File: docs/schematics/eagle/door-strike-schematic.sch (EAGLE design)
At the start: 9 parts, among them T1 TIP120

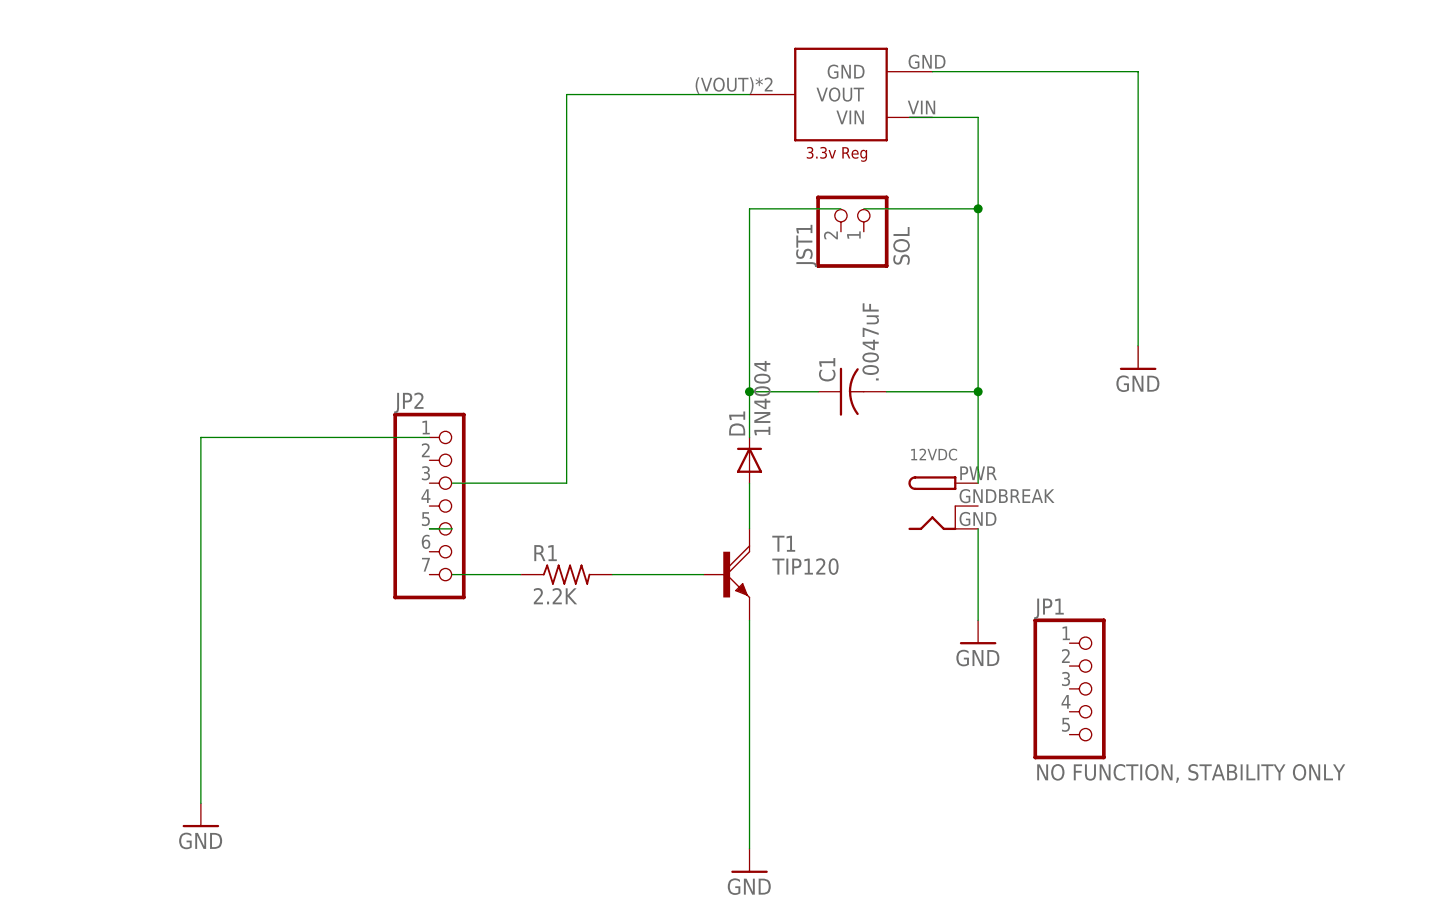
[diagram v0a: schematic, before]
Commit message: updated schema with RFduino component and caps for voltage regulation
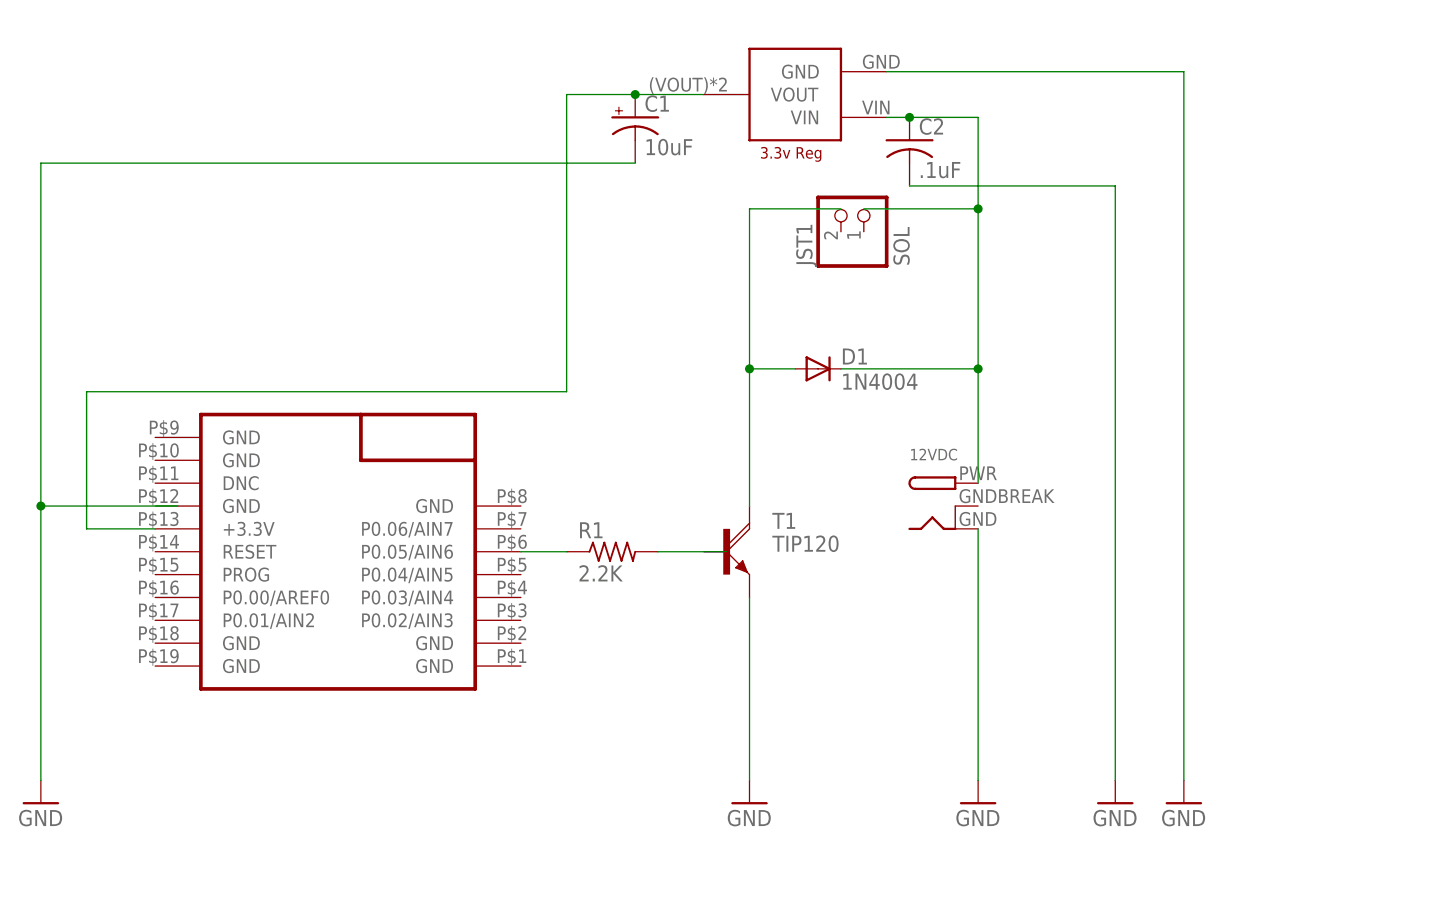
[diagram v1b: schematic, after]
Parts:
- removed JP1: NO FUNCTION, STABILITY ONLY, pinhead:PINHD-1X5
- removed JP2: (no value), pinhead:PINHD-1X7
- added C2: .1uF, adafruit:C-US102-054X133
- added U$2: RFD22301, RFD22301-11.25.13:RFD22301
- C1: value .0047uF -> 10uF; device adafruit:C-US025-024X044 -> adafruit:CPOL-USE2-5
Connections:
- removed net N$5: JP2.5
- removed net N$6 (its old number): C1.1, D1.C
- net GND: now also C1.-, C2.2; no longer JP2.1
- net N$1: now also R1.1, U$2.P0.05/AIN6; no longer R1.2, T1.B
- net N$2: now also R1.2; no longer R1.1
- net N$7: now also C1.+, U$2.+3.3V
- net N$8: now also C2.1, D1.C, U$1.VIN; no longer C1.2
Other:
- moved on the sheet: D1, R1, T1
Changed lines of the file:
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@@
 <part name="JST1" library="adafruit" deviceset="JST_2PIN" device="-THM" value="SOL"/>
 <part name="GND1" library="supply1" deviceset="GND" device=""/>
-<part name="JP1" library="pinhead" deviceset="PINHD-1X5" device="" value="NO FUNCTION, STABILITY ONLY"/>
-<part name="JP2" library="pinhead" deviceset="PINHD-1X7" device=""/>
 <part name="GND2" library="supply1" deviceset="GND" device=""/>
 <part name="12VDC" library="adafruit" deviceset="DCBARREL" device="PTH"/>
@@
 <part name="GND3" library="supply1" deviceset="GND" device=""/>
 <part name="GND4" library="supply1" deviceset="GND" device=""/>
-<part name="C1" library="adafruit" deviceset="C-US" device="025-024X044" value=".0047uF"/>
+<part name="C1" library="adafruit" deviceset="CPOL-US" device="E2-5" value="10uF"/>
+<part name="C2" library="adafruit" deviceset="C-US" device="102-054X133" value=".1uF"/>
+<part name="GND5" library="supply1" deviceset="GND" device=""/>
+<part name="U$2" library="RFD22301-11.25.13" deviceset="RFD22301" device=""/>
 </parts>
 <sheets>
@@
 </plain>
 <instances>
-<instance part="T1" gate="1" x="48.26" y="50.8"/>
-<instance part="R1" gate="G$1" x="30.48" y="50.8"/>
-<instance part="D1" gate="1" x="50.8" y="63.5" rot="R90"/>
+<instance part="T1" gate="1" x="48.26" y="53.34"/>
+<instance part="R1" gate="G$1" x="35.56" y="53.34"/>
+<instance part="D1" gate="1" x="58.42" y="73.66"/>
 <instance part="JST1" gate="G$1" x="63.5" y="91.44" rot="R90"/>
-<instance part="GND1" gate="1" x="50.8" y="17.78"/>
-<instance part="JP1" gate="A" x="88.9" y="38.1"/>
-<instance part="JP2" gate="A" x="17.78" y="58.42"/>
-<instance part="GND2" gate="1" x="-10.16" y="22.86"/>
+<instance part="GND1" gate="1" x="50.8" y="25.4"/>
+<instance part="GND2" gate="1" x="-27.94" y="25.4"/>
 <instance part="12VDC" gate="G$1" x="73.66" y="58.42"/>
-<instance part="U$1" gate="G$1" x="60.96" y="104.14" rot="R180"/>
-<instance part="GND3" gate="1" x="93.98" y="73.66"/>
-<instance part="GND4" gate="1" x="76.2" y="43.18"/>
-<instance part="C1" gate="G$1" x="60.96" y="71.12" rot="R90"/>
+<instance part="U$1" gate="G$1" x="55.88" y="104.14" rot="R180"/>
+<instance part="GND3" gate="1" x="99.06" y="25.4"/>
+<instance part="GND4" gate="1" x="76.2" y="25.4"/>
+<instance part="C1" gate="G$1" x="38.1" y="101.6"/>
+<instance part="C2" gate="G$1" x="68.58" y="99.06"/>
+<instance part="GND5" gate="1" x="91.44" y="25.4"/>
+<instance part="U$2" gate="G$1" x="5.08" y="53.34" rot="R180"/>
 </instances>
 <busses>
 </busses>
 <nets>
-<net name="N$1" class="0">
-<segment>
-<pinref part="R1" gate="G$1" pin="2"/>
-<pinref part="T1" gate="1" pin="B"/>
-<wire x1="35.56" y1="50.8" x2="45.72" y2="50.8" width="0.1524" layer="91"/>
-</segment>
-</net>
 <net name="GND" class="0">
 <segment>
 <pinref part="T1" gate="1" pin="E"/>
 <pinref part="GND1" gate="1" pin="GND"/>
-<wire x1="50.8" y1="45.72" x2="50.8" y2="20.32" width="0.1524" layer="91"/>
+<wire x1="50.8" y1="48.26" x2="50.8" y2="27.94" width="0.1524" layer="91"/>
 </segment>
 <segment>
 <pinref part="GND2" gate="1" pin="GND"/>
-<wire x1="-10.16" y1="25.4" x2="-10.16" y2="66.04" width="0.1524" layer="91"/>
-<pinref part="JP2" gate="A" pin="1"/>
-<wire x1="-10.16" y1="66.04" x2="15.24" y2="66.04" width="0.1524" layer="91"/>
+<wire x1="-27.94" y1="27.94" x2="-27.94" y2="58.42" width="0.1524" layer="91"/>
+<pinref part="C1" gate="G$1" pin="-"/>
+<wire x1="-27.94" y1="58.42" x2="-27.94" y2="96.52" width="0.1524" layer="91"/>
+<wire x1="38.1" y1="96.52" x2="-27.94" y2="96.52" width="0.1524" layer="91"/>
+<wire x1="-27.94" y1="58.42" x2="-12.7" y2="58.42" width="0.1524" layer="91"/>
+<junction x="-27.94" y="58.42"/>
 </segment>
 <segment>
 <pinref part="U$1" gate="G$1" pin="GND"/>
-<wire x1="71.12" y1="106.68" x2="93.98" y2="106.68" width="0.1524" layer="91"/>
-<wire x1="93.98" y1="106.68" x2="93.98" y2="76.2" width="0.1524" layer="91"/>
+<wire x1="66.04" y1="106.68" x2="99.06" y2="106.68" width="0.1524" layer="91"/>
+<wire x1="99.06" y1="106.68" x2="99.06" y2="27.94" width="0.1524" layer="91"/>
 <pinref part="GND3" gate="1" pin="GND"/>
 </segment>
 <segment>
 <pinref part="12VDC" gate="G$1" pin="GND"/>
-<wire x1="76.2" y1="55.88" x2="76.2" y2="45.72" width="0.1524" layer="91"/>
+<wire x1="76.2" y1="55.88" x2="76.2" y2="27.94" width="0.1524" layer="91"/>
 <pinref part="GND4" gate="1" pin="GND"/>
 </segment>
-</net>
-<net name="N$3" class="0">
 <segment>
-<pinref part="T1" gate="1" pin="C"/>
-<pinref part="D1" gate="1" pin="A"/>
-<wire x1="50.8" y1="55.88" x2="50.8" y2="60.96" width="0.1524" layer="91"/>
+<pinref part="C2" gate="G$1" pin="2"/>
+<wire x1="68.58" y1="93.98" x2="91.44" y2="93.98" width="0.1524" layer="91"/>
+<wire x1="91.44" y1="93.98" x2="91.44" y2="27.94" width="0.1524" layer="91"/>
+<pinref part="GND5" gate="1" pin="GND"/>
 </segment>
 </net>
@@
 <segment>
 <pinref part="12VDC" gate="G$1" pin="PWR"/>
-<wire x1="76.2" y1="60.96" x2="76.2" y2="71.12" width="0.1524" layer="91"/>
-<wire x1="76.2" y1="71.12" x2="76.2" y2="91.44" width="0.1524" layer="91"/>
+<wire x1="76.2" y1="60.96" x2="76.2" y2="73.66" width="0.1524" layer="91"/>
+<wire x1="76.2" y1="73.66" x2="76.2" y2="91.44" width="0.1524" layer="91"/>
 <wire x1="63.5" y1="91.44" x2="76.2" y2="91.44" width="0.1524" layer="91"/>
-<wire x1="76.2" y1="91.44" x2="76.2" y2="101.6" width="0.1524" layer="91"/>
+<pinref part="U$1" gate="G$1" pin="VIN"/>
+<wire x1="66.04" y1="101.6" x2="68.58" y2="101.6" width="0.1524" layer="91"/>
+<wire x1="68.58" y1="101.6" x2="76.2" y2="101.6" width="0.1524" layer="91"/>
+<wire x1="76.2" y1="101.6" x2="76.2" y2="91.44" width="0.1524" layer="91"/>
 <junction x="76.2" y="91.44"/>
-<wire x1="76.2" y1="101.6" x2="68.58" y2="101.6" width="0.1524" layer="91"/>
-<pinref part="C1" gate="G$1" pin="2"/>
-<wire x1="66.04" y1="71.12" x2="76.2" y2="71.12" width="0.1524" layer="91"/>
-<junction x="76.2" y="71.12"/>
-</segment>
-</net>
-<net name="N$2" class="0">
-<segment>
-<pinref part="R1" gate="G$1" pin="1"/>
-<wire x1="25.4" y1="50.8" x2="17.78" y2="50.8" width="0.1524" layer="91"/>
-</segment>
-</net>
-<net name="N$5" class="0">
-<segment>
-<wire x1="17.78" y1="55.88" x2="15.24" y2="55.88" width="0.1524" layer="91"/>
-<pinref part="JP2" gate="A" pin="5"/>
+<pinref part="C2" gate="G$1" pin="1"/>
+<junction x="68.58" y="101.6"/>
+<pinref part="D1" gate="1" pin="C"/>
+<wire x1="60.96" y1="73.66" x2="76.2" y2="73.66" width="0.1524" layer="91"/>
+<junction x="76.2" y="73.66"/>
 </segment>
 </net>
@@
 <segment>
 <pinref part="U$1" gate="G$1" pin="VOUT"/>
-<wire x1="50.8" y1="104.14" x2="30.48" y2="104.14" width="0.1524" layer="91"/>
-<wire x1="30.48" y1="104.14" x2="30.48" y2="60.96" width="0.1524" layer="91"/>
-<wire x1="30.48" y1="60.96" x2="17.78" y2="60.96" width="0.1524" layer="91"/>
+<wire x1="45.72" y1="104.14" x2="38.1" y2="104.14" width="0.1524" layer="91"/>
+<wire x1="38.1" y1="104.14" x2="30.48" y2="104.14" width="0.1524" layer="91"/>
+<wire x1="30.48" y1="104.14" x2="30.48" y2="71.12" width="0.1524" layer="91"/>
+<pinref part="C1" gate="G$1" pin="+"/>
+<junction x="38.1" y="104.14"/>
+<wire x1="30.48" y1="71.12" x2="-22.86" y2="71.12" width="0.1524" layer="91"/>
+<wire x1="-22.86" y1="71.12" x2="-22.86" y2="55.88" width="0.1524" layer="91"/>
+<pinref part="U$2" gate="G$1" pin="+3.3V"/>
+<wire x1="-22.86" y1="55.88" x2="-15.24" y2="55.88" width="0.1524" layer="91"/>
 </segment>
 </net>
@@
 <segment>
 <wire x1="50.8" y1="91.44" x2="60.96" y2="91.44" width="0.1524" layer="91"/>
-<pinref part="D1" gate="1" pin="C"/>
-<wire x1="50.8" y1="66.04" x2="50.8" y2="71.12" width="0.1524" layer="91"/>
-<pinref part="C1" gate="G$1" pin="1"/>
-<wire x1="50.8" y1="71.12" x2="50.8" y2="91.44" width="0.1524" layer="91"/>
-<wire x1="58.42" y1="71.12" x2="50.8" y2="71.12" width="0.1524" layer="91"/>
-<junction x="50.8" y="71.12"/>
+<pinref part="T1" gate="1" pin="C"/>
+<wire x1="50.8" y1="91.44" x2="50.8" y2="73.66" width="0.1524" layer="91"/>
+<pinref part="D1" gate="1" pin="A"/>
+<wire x1="50.8" y1="73.66" x2="50.8" y2="58.42" width="0.1524" layer="91"/>
+<wire x1="50.8" y1="73.66" x2="55.88" y2="73.66" width="0.1524" layer="91"/>
+<junction x="50.8" y="73.66"/>
 </segment>
 </net>
+<net name="N$1" class="0">
+<segment>
+<pinref part="R1" gate="G$1" pin="1"/>
+<pinref part="U$2" gate="G$1" pin="P0.05/AIN6"/>
+<wire x1="30.48" y1="53.34" x2="25.4" y2="53.34" width="0.1524" layer="91"/>
+</segment>
+</net>
+<net name="N$2" class="0">
+<segment>
+<pinref part="R1" gate="G$1" pin="2"/>
+<wire x1="40.64" y1="53.34" x2="48.26" y2="53.34" width="0.1524" layer="91"/>
+</segment>
+</net>

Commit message: cleaned up board organization and added label for LD1117 IC
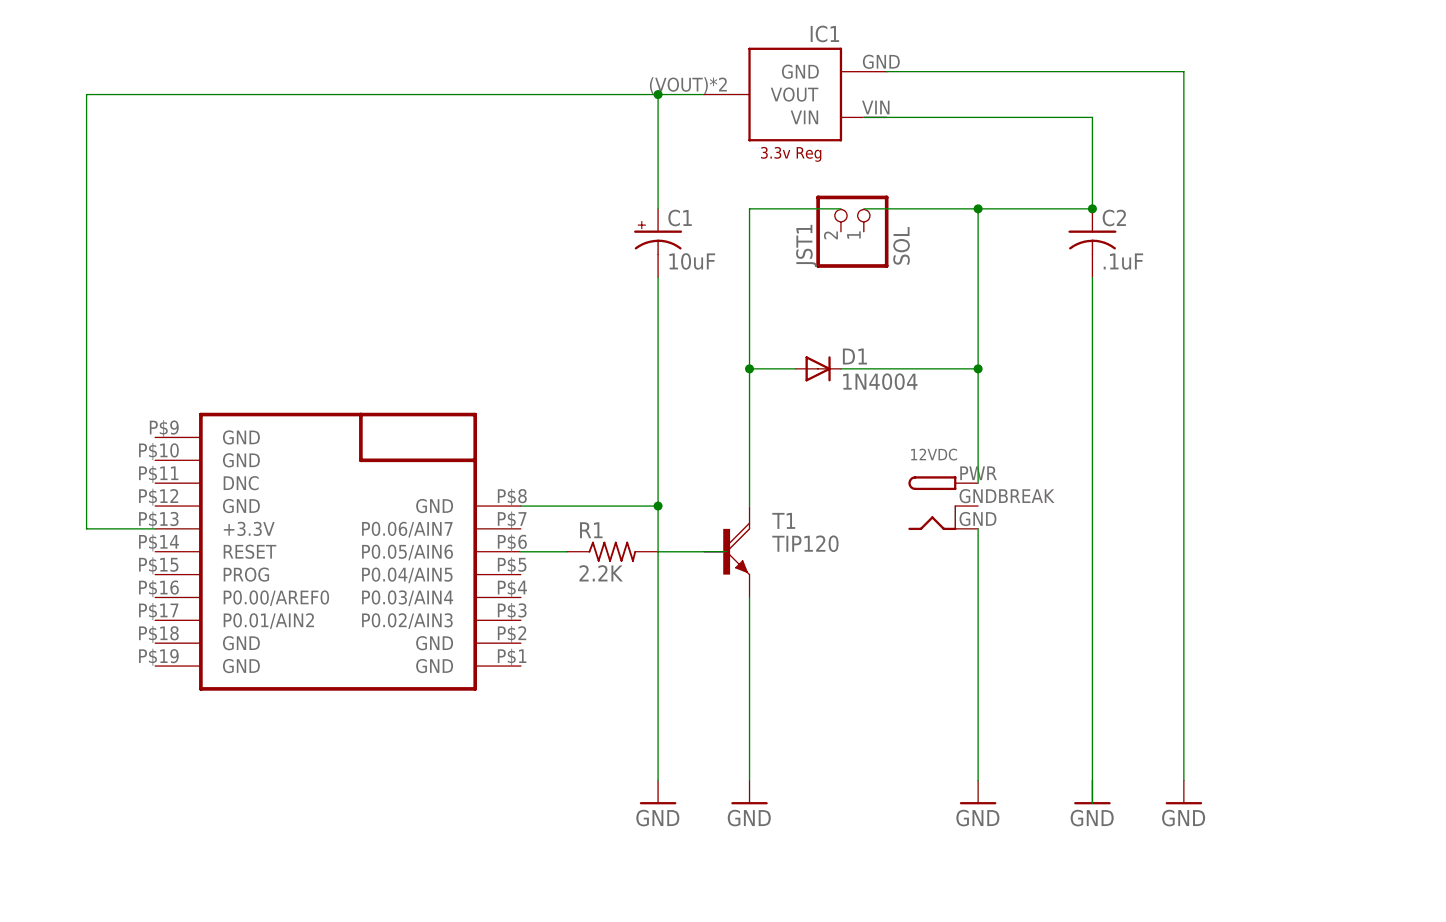
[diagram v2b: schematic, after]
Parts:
- renumbered U$1 to IC1
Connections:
- net GND: now also U$2.GND@3
- net N$8: no longer IC1.VIN
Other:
- moved on the sheet: C1, C2
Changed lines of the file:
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@@
 <?xml version="1.0" encoding="utf-8"?>
 <!DOCTYPE eagle SYSTEM "eagle.dtd">
-<eagle version="7.2.0">
+<eagle version="7.3.0">
 <drawing>
 <settings>
@@
 <part name="GND2" library="supply1" deviceset="GND" device=""/>
 <part name="12VDC" library="adafruit" deviceset="DCBARREL" device="PTH"/>
-<part name="U$1" library="LD1117" deviceset="LD1117" device=""/>
+<part name="IC1" library="LD1117" deviceset="LD1117" device=""/>
 <part name="GND3" library="supply1" deviceset="GND" device=""/>
 <part name="GND4" library="supply1" deviceset="GND" device=""/>
@@
 <instance part="JST1" gate="G$1" x="63.5" y="91.44" rot="R90"/>
 <instance part="GND1" gate="1" x="50.8" y="25.4"/>
-<instance part="GND2" gate="1" x="-27.94" y="25.4"/>
+<instance part="GND2" gate="1" x="40.64" y="25.4"/>
 <instance part="12VDC" gate="G$1" x="73.66" y="58.42"/>
-<instance part="U$1" gate="G$1" x="55.88" y="104.14" rot="R180"/>
+<instance part="IC1" gate="G$1" x="55.88" y="104.14" rot="R180"/>
 <instance part="GND3" gate="1" x="99.06" y="25.4"/>
 <instance part="GND4" gate="1" x="76.2" y="25.4"/>
-<instance part="C1" gate="G$1" x="38.1" y="101.6"/>
-<instance part="C2" gate="G$1" x="68.58" y="99.06"/>
-<instance part="GND5" gate="1" x="91.44" y="25.4"/>
+<instance part="C1" gate="G$1" x="40.64" y="88.9"/>
+<instance part="C2" gate="G$1" x="88.9" y="88.9"/>
+<instance part="GND5" gate="1" x="88.9" y="25.4"/>
 <instance part="U$2" gate="G$1" x="5.08" y="53.34" rot="R180"/>
 </instances>
@@
 </segment>
 <segment>
-<pinref part="GND2" gate="1" pin="GND"/>
-<wire x1="-27.94" y1="27.94" x2="-27.94" y2="58.42" width="0.1524" layer="91"/>
-<pinref part="C1" gate="G$1" pin="-"/>
-<wire x1="-27.94" y1="58.42" x2="-27.94" y2="96.52" width="0.1524" layer="91"/>
-<wire x1="38.1" y1="96.52" x2="-27.94" y2="96.52" width="0.1524" layer="91"/>
-<wire x1="-27.94" y1="58.42" x2="-12.7" y2="58.42" width="0.1524" layer="91"/>
-<junction x="-27.94" y="58.42"/>
-</segment>
-<segment>
-<pinref part="U$1" gate="G$1" pin="GND"/>
+<pinref part="IC1" gate="G$1" pin="GND"/>
 <wire x1="66.04" y1="106.68" x2="99.06" y2="106.68" width="0.1524" layer="91"/>
 <wire x1="99.06" y1="106.68" x2="99.06" y2="27.94" width="0.1524" layer="91"/>
@@
 </segment>
 <segment>
+<pinref part="U$2" gate="G$1" pin="GND@3"/>
+<wire x1="25.4" y1="58.42" x2="40.64" y2="58.42" width="0.1524" layer="91"/>
+<pinref part="C1" gate="G$1" pin="-"/>
+<wire x1="40.64" y1="83.82" x2="40.64" y2="58.42" width="0.1524" layer="91"/>
+<pinref part="GND2" gate="1" pin="GND"/>
+<wire x1="40.64" y1="58.42" x2="40.64" y2="27.94" width="0.1524" layer="91"/>
+<junction x="40.64" y="58.42"/>
+</segment>
+<segment>
 <pinref part="C2" gate="G$1" pin="2"/>
-<wire x1="68.58" y1="93.98" x2="91.44" y2="93.98" width="0.1524" layer="91"/>
-<wire x1="91.44" y1="93.98" x2="91.44" y2="27.94" width="0.1524" layer="91"/>
-<pinref part="GND5" gate="1" pin="GND"/>
+<wire x1="88.9" y1="83.82" x2="88.9" y2="25.4" width="0.1524" layer="91"/>
 </segment>
 </net>
@@
 <wire x1="76.2" y1="73.66" x2="76.2" y2="91.44" width="0.1524" layer="91"/>
 <wire x1="63.5" y1="91.44" x2="76.2" y2="91.44" width="0.1524" layer="91"/>
-<pinref part="U$1" gate="G$1" pin="VIN"/>
-<wire x1="66.04" y1="101.6" x2="68.58" y2="101.6" width="0.1524" layer="91"/>
-<wire x1="68.58" y1="101.6" x2="76.2" y2="101.6" width="0.1524" layer="91"/>
-<wire x1="76.2" y1="101.6" x2="76.2" y2="91.44" width="0.1524" layer="91"/>
-<junction x="76.2" y="91.44"/>
-<pinref part="C2" gate="G$1" pin="1"/>
-<junction x="68.58" y="101.6"/>
 <pinref part="D1" gate="1" pin="C"/>
 <wire x1="60.96" y1="73.66" x2="76.2" y2="73.66" width="0.1524" layer="91"/>
 <junction x="76.2" y="73.66"/>
+<pinref part="C2" gate="G$1" pin="1"/>
+<wire x1="76.2" y1="91.44" x2="88.9" y2="91.44" width="0.1524" layer="91"/>
+<junction x="76.2" y="91.44"/>
+<wire x1="63.5" y1="101.6" x2="88.9" y2="101.6" width="0.1524" layer="91"/>
+<wire x1="88.9" y1="101.6" x2="88.9" y2="91.44" width="0.1524" layer="91"/>
+<junction x="88.9" y="91.44"/>
 </segment>
 </net>
 <net name="N$7" class="0">
 <segment>
-<pinref part="U$1" gate="G$1" pin="VOUT"/>
-<wire x1="45.72" y1="104.14" x2="38.1" y2="104.14" width="0.1524" layer="91"/>
-<wire x1="38.1" y1="104.14" x2="30.48" y2="104.14" width="0.1524" layer="91"/>
-<wire x1="30.48" y1="104.14" x2="30.48" y2="71.12" width="0.1524" layer="91"/>
-<pinref part="C1" gate="G$1" pin="+"/>
-<junction x="38.1" y="104.14"/>
-<wire x1="30.48" y1="71.12" x2="-22.86" y2="71.12" width="0.1524" layer="91"/>
-<wire x1="-22.86" y1="71.12" x2="-22.86" y2="55.88" width="0.1524" layer="91"/>
+<wire x1="-22.86" y1="104.14" x2="-22.86" y2="55.88" width="0.1524" layer="91"/>
 <pinref part="U$2" gate="G$1" pin="+3.3V"/>
 <wire x1="-22.86" y1="55.88" x2="-15.24" y2="55.88" width="0.1524" layer="91"/>
+<pinref part="IC1" gate="G$1" pin="VOUT"/>
+<wire x1="45.72" y1="104.14" x2="40.64" y2="104.14" width="0.1524" layer="91"/>
+<pinref part="C1" gate="G$1" pin="+"/>
+<wire x1="40.64" y1="104.14" x2="-22.86" y2="104.14" width="0.1524" layer="91"/>
+<wire x1="40.64" y1="91.44" x2="40.64" y2="104.14" width="0.1524" layer="91"/>
+<junction x="40.64" y="104.14"/>
 </segment>
 </net>
